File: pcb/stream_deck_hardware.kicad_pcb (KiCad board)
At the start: 2 copper layers, 70 x 100 mm, 103 parts, among them J2 USB_C_Receptacle_USB2.0, J3 Conn_01x04_Male, J4 Conn_01x04_Male, J5 Conn_01x05_Male, J6 Conn_01x03_Female, SW1 SW_Push, SW2 SW_Push, SW3 SW_Push, SW4 SW_Push, SW5 SW_Push, SW6 SW_Push, SW7 SW_Push, SW8 SW_Push, SW9 SW_Push, U1 LF33_TO252, U2 STM32F401RCTx, U3 74LVC1G332, U4 AT24CS02-STUM, U5 AT24CS02-STUM, Y1 Crystal_Small

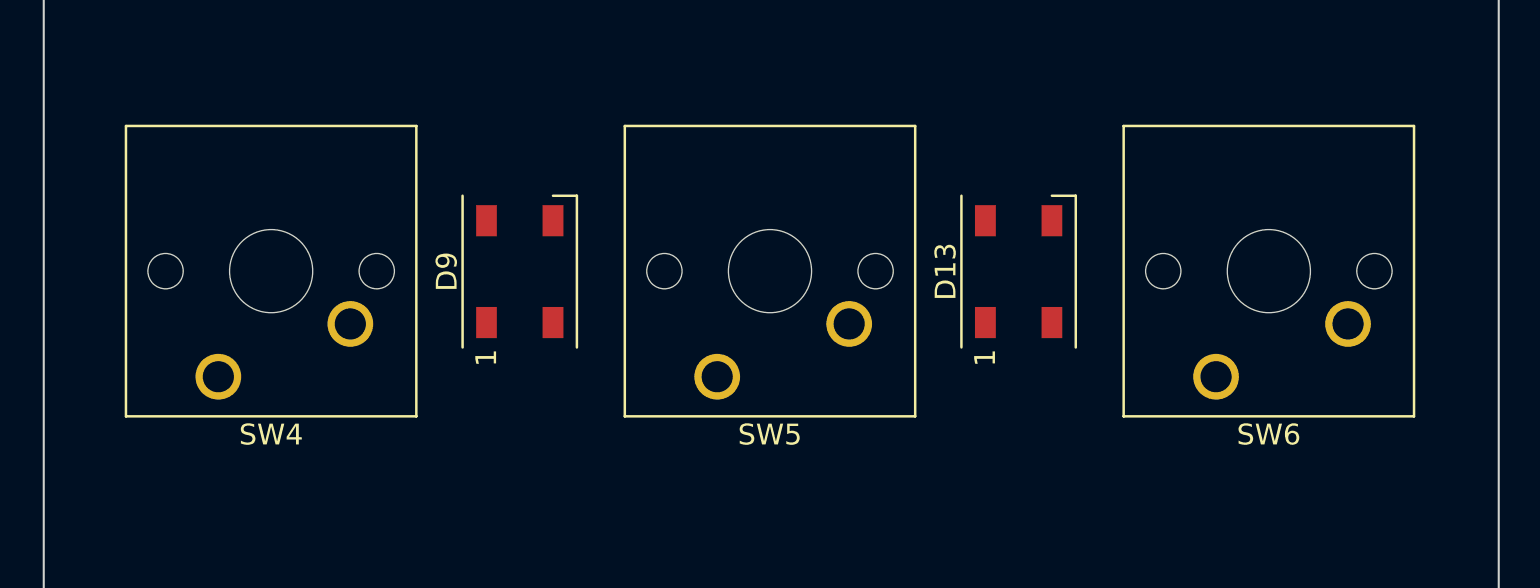
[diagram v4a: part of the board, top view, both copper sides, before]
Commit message: Components placement, added 3d model of cherry mx switch
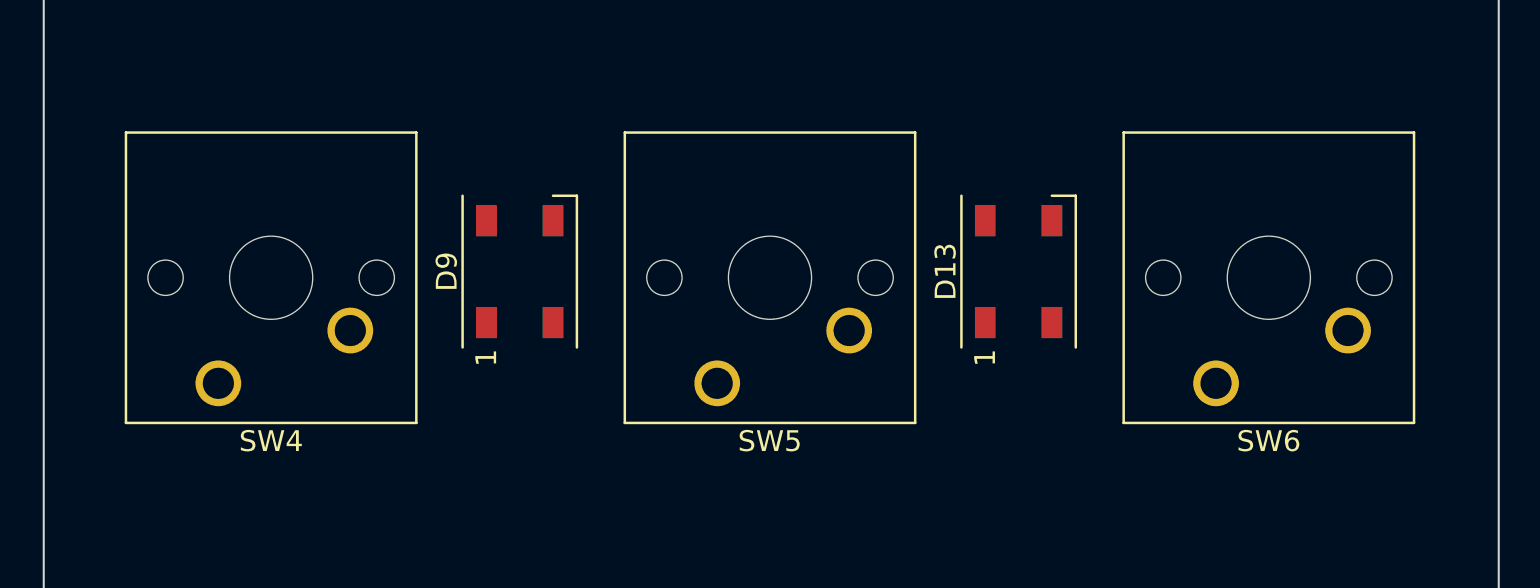
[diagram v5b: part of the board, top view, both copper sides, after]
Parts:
- SW1: value SW_Push -> SW_Push1
- SW2: value SW_Push -> SW_Push2
- SW3: value SW_Push -> SW_Push3
- moved SW4 0.32 mm to (63.0, 113.4)
- moved SW5 0.32 mm to (87.0, 113.4)
- moved SW6 0.32 mm to (111.0, 113.4)

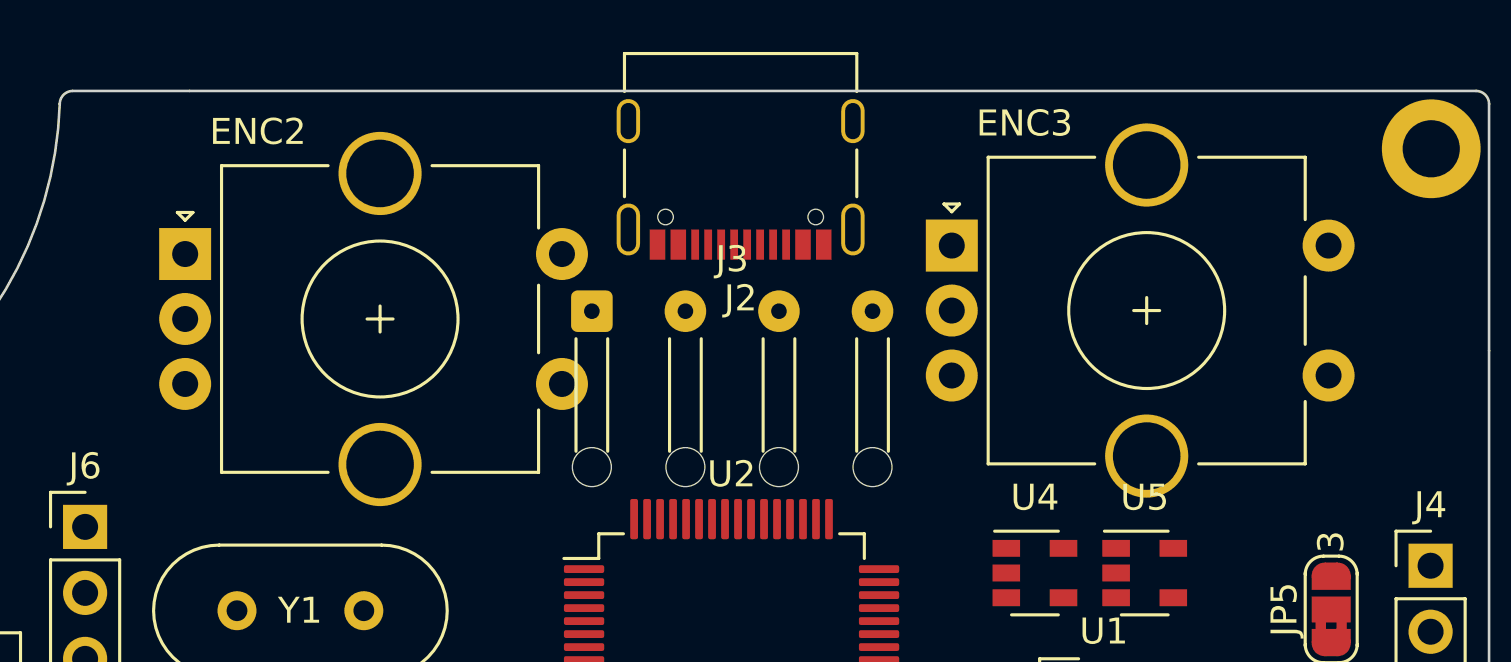
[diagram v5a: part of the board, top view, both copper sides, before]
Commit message: Remove usb wire connector
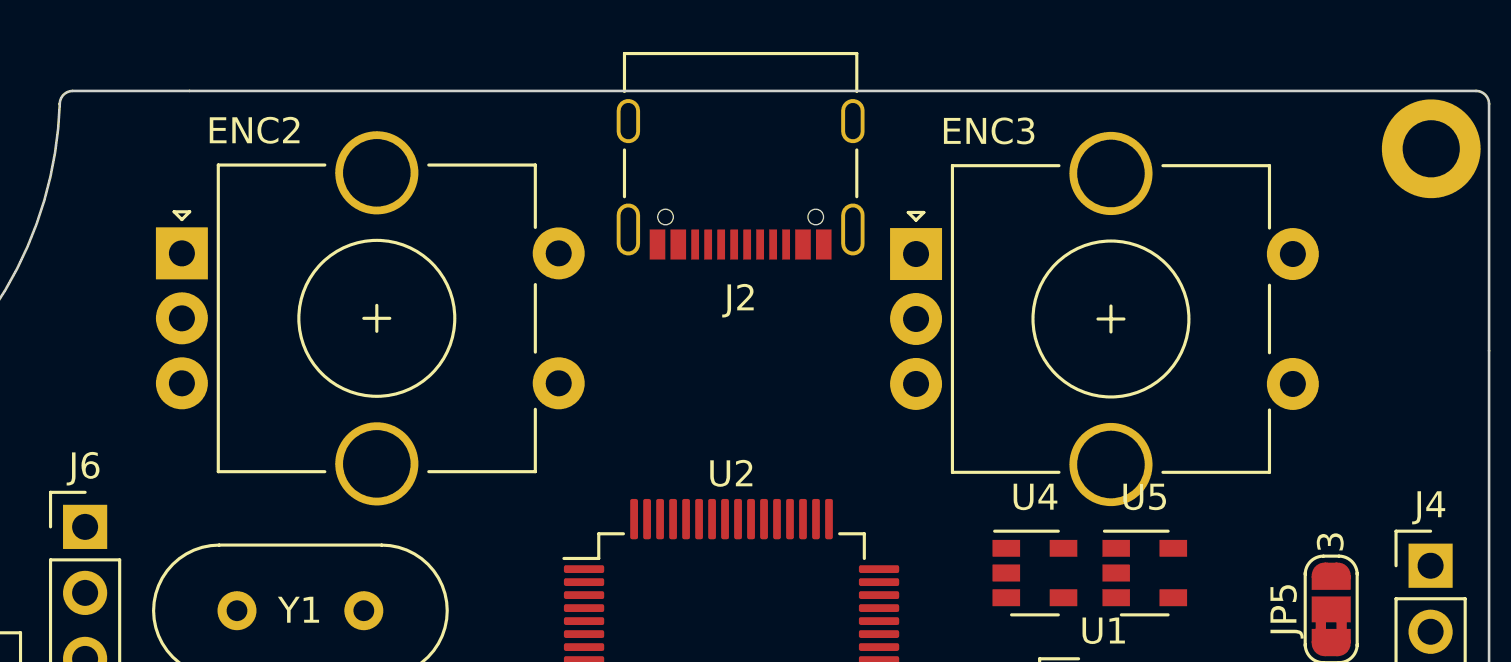
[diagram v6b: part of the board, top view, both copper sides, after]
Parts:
- removed J3: Conn_01x04_Male, Connector_Wire:SolderWire-0.1sqmm_1x04_P3.6mm_D0.4mm_OD1mm_Relief
- moved ENC3 1.41 mm to (102.5, 51.3)
- moved ENC2 0.13 mm to (74.3, 51.3)
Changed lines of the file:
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@@
     (tracks 0)
     (zones 0)
-    (modules 103)
+    (modules 102)
     (nets 82)
   )
@@
     )
   )
-  (module Connector_Wire:SolderWire-0.1sqmm_1x04_P3.6mm_D0.4mm_OD1mm_Relief (layer F.Cu)
-    (at 90.075 53.525)
-    (descr "Soldered wire connection with feed through strain relief, for 4 times 0.1 mm² wires, basic insulation, conductor diameter 0.4mm, outer diameter 1mm, size source Multi-Contact FLEXI-E 0.1 (https://ec.staubli.com/AcroFiles/Catalogues/TM_Cab-Main-11014119_(en)_hi.pdf), bend radius 3 times outer diameter, generated with kicad-footprint-generator")
-    (tags "connector wire 0.1sqmm strain-relief")
-    (attr virtual)
-    (fp_text reference J3 (at 5.4 -2) (layer F.SilkS)
-      (effects (font (size 1 1) (thickness 0.15)))
-    )
-    (fp_text value Conn_01x04_Male (at 5.4 7.95) (layer F.Fab)
-      (effects (font (size 1 1) (thickness 0.15)))
-    )
-    (fp_line (start 12.1 4.75) (end 9.5 4.75) (layer B.CrtYd) (width 0.05))
-    (fp_line (start 12.1 7.25) (end 12.1 4.75) (layer B.CrtYd) (width 0.05))
-    (fp_line (start 9.5 7.25) (end 12.1 7.25) (layer B.CrtYd) (width 0.05))
-    (fp_line (start 9.5 4.75) (end 9.5 7.25) (layer B.CrtYd) (width 0.05))
-    (fp_line (start 12.1 -1.3) (end 9.5 -1.3) (layer F.CrtYd) (width 0.05))
-    (fp_line (start 12.1 7.25) (end 12.1 -1.3) (layer F.CrtYd) (width 0.05))
-    (fp_line (start 9.5 7.25) (end 12.1 7.25) (layer F.CrtYd) (width 0.05))
-    (fp_line (start 9.5 -1.3) (end 9.5 7.25) (layer F.CrtYd) (width 0.05))
-    (fp_line (start 10.19 1.06) (end 10.19 5.39) (layer F.SilkS) (width 0.12))
-    (fp_line (start 11.41 1.06) (end 11.41 5.39) (layer F.SilkS) (width 0.12))
-    (fp_line (start 11.3 0) (end 11.3 6) (layer F.Fab) (width 0.1))
-    (fp_line (start 10.3 0) (end 10.3 6) (layer F.Fab) (width 0.1))
-    (fp_line (start 8.5 4.75) (end 5.9 4.75) (layer B.CrtYd) (width 0.05))
-    (fp_line (start 8.5 7.25) (end 8.5 4.75) (layer B.CrtYd) (width 0.05))
-    (fp_line (start 5.9 7.25) (end 8.5 7.25) (layer B.CrtYd) (width 0.05))
-    (fp_line (start 5.9 4.75) (end 5.9 7.25) (layer B.CrtYd) (width 0.05))
-    (fp_line (start 8.5 -1.3) (end 5.9 -1.3) (layer F.CrtYd) (width 0.05))
-    (fp_line (start 8.5 7.25) (end 8.5 -1.3) (layer F.CrtYd) (width 0.05))
-    (fp_line (start 5.9 7.25) (end 8.5 7.25) (layer F.CrtYd) (width 0.05))
-    (fp_line (start 5.9 -1.3) (end 5.9 7.25) (layer F.CrtYd) (width 0.05))
-    (fp_line (start 6.59 1.06) (end 6.59 5.39) (layer F.SilkS) (width 0.12))
-    (fp_line (start 7.81 1.06) (end 7.81 5.39) (layer F.SilkS) (width 0.12))
-    (fp_line (start 7.7 0) (end 7.7 6) (layer F.Fab) (width 0.1))
-    (fp_line (start 6.7 0) (end 6.7 6) (layer F.Fab) (width 0.1))
-    (fp_line (start 4.9 4.75) (end 2.3 4.75) (layer B.CrtYd) (width 0.05))
-    (fp_line (start 4.9 7.25) (end 4.9 4.75) (layer B.CrtYd) (width 0.05))
-    (fp_line (start 2.3 7.25) (end 4.9 7.25) (layer B.CrtYd) (width 0.05))
-    (fp_line (start 2.3 4.75) (end 2.3 7.25) (layer B.CrtYd) (width 0.05))
-    (fp_line (start 4.9 -1.3) (end 2.3 -1.3) (layer F.CrtYd) (width 0.05))
-    (fp_line (start 4.9 7.25) (end 4.9 -1.3) (layer F.CrtYd) (width 0.05))
-    (fp_line (start 2.3 7.25) (end 4.9 7.25) (layer F.CrtYd) (width 0.05))
-    (fp_line (start 2.3 -1.3) (end 2.3 7.25) (layer F.CrtYd) (width 0.05))
-    (fp_line (start 2.99 1.06) (end 2.99 5.39) (layer F.SilkS) (width 0.12))
-    (fp_line (start 4.21 1.06) (end 4.21 5.39) (layer F.SilkS) (width 0.12))
-    (fp_line (start 4.1 0) (end 4.1 6) (layer F.Fab) (width 0.1))
-    (fp_line (start 3.1 0) (end 3.1 6) (layer F.Fab) (width 0.1))
-    (fp_line (start 1.3 4.75) (end -1.3 4.75) (layer B.CrtYd) (width 0.05))
-    (fp_line (start 1.3 7.25) (end 1.3 4.75) (layer B.CrtYd) (width 0.05))
-    (fp_line (start -1.3 7.25) (end 1.3 7.25) (layer B.CrtYd) (width 0.05))
-    (fp_line (start -1.3 4.75) (end -1.3 7.25) (layer B.CrtYd) (width 0.05))
-    (fp_line (start 1.3 -1.3) (end -1.3 -1.3) (layer F.CrtYd) (width 0.05))
-    (fp_line (start 1.3 7.25) (end 1.3 -1.3) (layer F.CrtYd) (width 0.05))
-    (fp_line (start -1.3 7.25) (end 1.3 7.25) (layer F.CrtYd) (width 0.05))
-    (fp_line (start -1.3 -1.3) (end -1.3 7.25) (layer F.CrtYd) (width 0.05))
-    (fp_line (start -0.61 1.06) (end -0.61 5.39) (layer F.SilkS) (width 0.12))
-    (fp_line (start 0.61 1.06) (end 0.61 5.39) (layer F.SilkS) (width 0.12))
-    (fp_line (start 0.5 0) (end 0.5 6) (layer F.Fab) (width 0.1))
-    (fp_line (start -0.5 0) (end -0.5 6) (layer F.Fab) (width 0.1))
-    (fp_circle (center 10.8 6) (end 11.3 6) (layer F.Fab) (width 0.1))
-    (fp_circle (center 10.8 0) (end 11.3 0) (layer F.Fab) (width 0.1))
-    (fp_circle (center 7.2 6) (end 7.7 6) (layer F.Fab) (width 0.1))
-    (fp_circle (center 7.2 0) (end 7.7 0) (layer F.Fab) (width 0.1))
-    (fp_circle (center 3.6 6) (end 4.1 6) (layer F.Fab) (width 0.1))
-    (fp_circle (center 3.6 0) (end 4.1 0) (layer F.Fab) (width 0.1))
-    (fp_circle (center 0 6) (end 0.5 6) (layer F.Fab) (width 0.1))
-    (fp_circle (center 0 0) (end 0.5 0) (layer F.Fab) (width 0.1))
-    (fp_text user %R (at 5.4 3 90) (layer F.Fab)
-      (effects (font (size 0.8 0.8) (thickness 0.12)))
-    )
-    (pad "" np_thru_hole circle (at 10.8 6) (size 1.5 1.5) (drill 1.5) (layers *.Cu *.Mask))
-    (pad "" np_thru_hole circle (at 7.2 6) (size 1.5 1.5) (drill 1.5) (layers *.Cu *.Mask))
-    (pad "" np_thru_hole circle (at 3.6 6) (size 1.5 1.5) (drill 1.5) (layers *.Cu *.Mask))
-    (pad "" np_thru_hole circle (at 0 6) (size 1.5 1.5) (drill 1.5) (layers *.Cu *.Mask))
-    (pad 4 thru_hole circle (at 10.8 0) (size 1.6 1.6) (drill 0.6) (layers *.Cu *.Mask)
-      (net 1 GND))
-    (pad 3 thru_hole circle (at 7.2 0) (size 1.6 1.6) (drill 0.6) (layers *.Cu *.Mask)
-      (net 26 USB_DP))
-    (pad 2 thru_hole circle (at 3.6 0) (size 1.6 1.6) (drill 0.6) (layers *.Cu *.Mask)
-      (net 27 USB_DM))
-    (pad 1 thru_hole roundrect (at 0 0) (size 1.6 1.6) (drill 0.6) (layers *.Cu *.Mask) (roundrect_rratio 0.15625)
-      (net 3 +5V))
-    (model ${KISYS3DMOD}/Connector_Wire.3dshapes/SolderWire-0.1sqmm_1x04_P3.6mm_D0.4mm_OD1mm_Relief.wrl
-      (at (xyz 0 0 0))
-      (scale (xyz 1 1 1))
-      (rotate (xyz 0 0 0))
-    )
-  )
   (module Jumper:SolderJumper-3_P1.3mm_Bridged2Bar12_RoundedPad1.0x1.5mm_NumberLabels (layer F.Cu)
     (at 118.525 65 90)
@@
   )
   (module Rotary_Encoder:RotaryEncoder_Alps_EC11E-Switch_Vertical_H20mm_CircularMountingHoles (layer F.Cu)
-    (at 103.925 51)
+    (at 102.55 51.325)
     (descr "Alps rotary encoder, EC12E... with switch, vertical shaft, mounting holes with circular drills, http://www.alps.com/prod/info/E/HTML/Encoder/Incremental/EC11/EC11E15204A3.html")
     (tags "rotary encoder")
@@
   )
   (module Rotary_Encoder:RotaryEncoder_Alps_EC11E-Switch_Vertical_H20mm_CircularMountingHoles (layer F.Cu)
-    (at 74.425 51.325)
+    (at 74.3 51.3)
     (descr "Alps rotary encoder, EC12E... with switch, vertical shaft, mounting holes with circular drills, http://www.alps.com/prod/info/E/HTML/Encoder/Incremental/EC11/EC11E15204A3.html")
     (tags "rotary encoder")

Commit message: Component placement
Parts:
- moved R4 181.9 mm to (94.0, 53.6), turned to 90 degrees
- moved R3 178.4 mm to (100.3, 53.6), turned to 270 degrees
- moved C11 150.5 mm to (74.7, 69.4), turned to 270 degrees
- moved C10 144.5 mm to (76.3, 69.4), turned to 270 degrees
